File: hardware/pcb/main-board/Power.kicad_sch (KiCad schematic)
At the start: 59 parts, among them J1 Battery 22.2V IN, J16 Motor Driver, J2 Power Switch, J3 GND Spare Headers, J4 +V Spare Headers, Q1 DMMT5401 PNP, Q2 SSM3J332R, Q3 DMG2305UX-EV, Q4 DMMT5401 PNP, SW1 SW_SPST, U1 3.3V Buck, U2 12V Buck, U3 MAX42403AFLB+

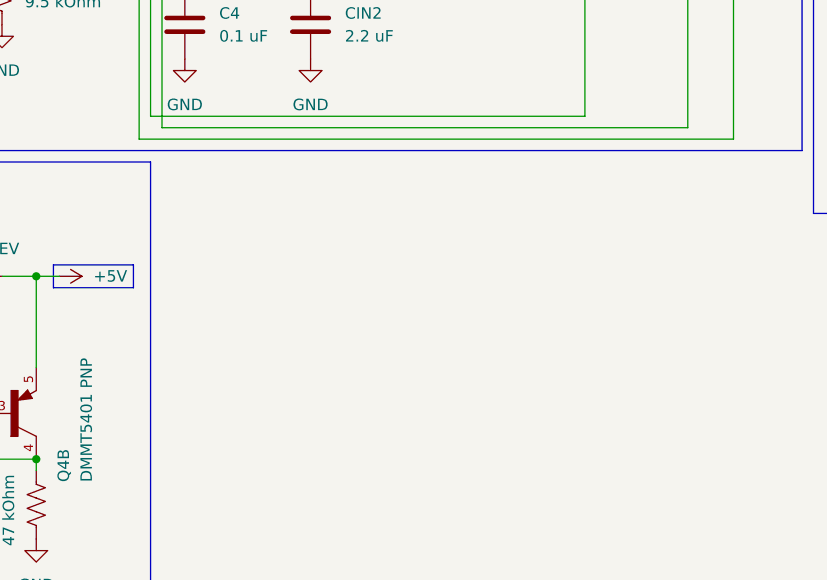
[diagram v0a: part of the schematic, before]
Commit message: Stepper drivers (real)
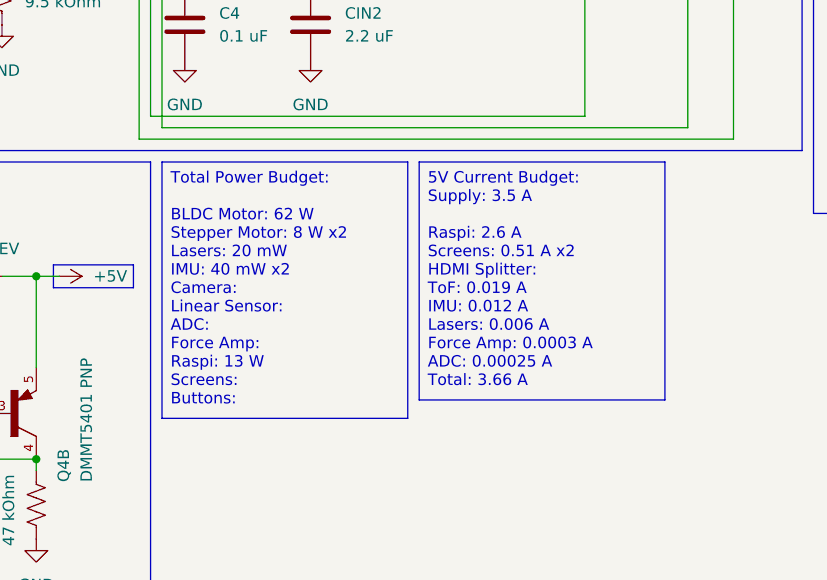
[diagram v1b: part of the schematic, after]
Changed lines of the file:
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@@
+		)
+	)
+	(text_box "Total Power Budget:\n\nBLDC Motor: 62 W\nStepper Motor: 8 W x2\nLasers: 20 mW\nIMU: 40 mW x2\nCamera:\nLinear Sensor:\nADC:\nForce Amp:\nRaspi: 13 W\nScreens:\nButtons:"
+		(exclude_from_sim no)
+		(at 58.42 124.46 0)
+		(size 27.305 28.4838)
+		(margins 0.9525 0.9525 0.9525 0.9525)
+		(stroke
+			(width 0)
+			(type solid)
+		)
+		(fill
+			(type none)
+		)
+		(effects
+			(font
+				(size 1.27 1.27)
+			)
+			(justify left top)
+		)
+	)
+	(text_box "5V Current Budget:\nSupply: 3.5 A\n\nRaspi: 2.6 A\nScreens: 0.51 A x2\nHDMI Splitter:\nToF: 0.019 A\nIMU: 0.012 A\nLasers: 0.006 A\nForce Amp: 0.0003 A\nADC: 0.00025 A\nTotal: 3.66 A"
+		(exclude_from_sim no)
+		(at 86.995 124.46 0)
+		(size 27.305 26.4392)
+		(margins 0.9525 0.9525 0.9525 0.9525)
+		(stroke
+			(width 0)
+			(type solid)
+		)
+		(fill
+			(type none)
+		)
+		(effects
+			(font
+				(size 1.27 1.27)
+			)
+			(justify left top)
 		)
 	)

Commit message: CAN-FD Transceiver Done
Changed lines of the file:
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@@
 		)
 	)
-	(text_box "5V Current Budget:\nSupply: 3.5 A\n\nRaspi: 2.6 A\nScreens: 0.51 A x2\nHDMI Splitter:\nToF: 0.019 A\nIMU: 0.012 A\nLasers: 0.006 A\nForce Amp: 0.0003 A\nADC: 0.00025 A\nTotal: 3.66 A"
+	(text_box "5V OLD Current Budget:\nSupply: 3.5 A\n\nRaspi: 2.6 A\nScreens: 0.51 A x2\nHDMI Splitter:\nToF: 0.019 A\nIMU: 0.012 A\nLasers: 0.006 A\nForce Amp: 0.0003 A\nADC: 0.00025 A\nTotal: 3.66 A"
 		(exclude_from_sim no)
 		(at 86.995 124.46 0)

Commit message: IMUs, I2C Pullups, Screen Power USB-C Ports
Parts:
- removed D6: SMCJ15A, Diode_SMD:D_SMC, symbol Device:D_Zener
- removed D7: SMCJ28A, Diode_SMD:D_SMC, symbol Device:D_Zener
- removed J2: Power Switch, Connector_AMASS:AMASS_XT30PW-F_1x02_P2.50mm_Horizontal, symbol Connector:Conn_01x02_Socket
- removed U2: 12V Buck, Converter_DCDC:Converter_DCDC_TRACO_TSR-1_THT, symbol Regulator_Switching:TSR_1-24120
- added J18: Screen 1 Power, symbol Connector:USB_C_Receptacle_PowerOnly_6P
- added J19: Screen 2 Power, symbol Connector:USB_C_Receptacle_PowerOnly_6P
- added R40, R41, R42, R43: 22 kOhm, Resistor_SMD:R_1206_3216Metric_Pad1.30x1.75mm_HandSolder, symbol Device:R_US
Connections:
- net +12V: no longer Contactor1.1, Flyback1.1 (K)
- net +5V: now also J18.A9 (VBUS), J18.B9 (VBUS), J19.A9 (VBUS), J19.B9 (VBUS), R40.2, R41.1, R42.1, R43.2
- net GND: now also J18.A12 (GND), J18.B12 (GND), J18.SH (SHIELD), J19.A12 (GND), J19.B12 (GND), J19.SH (SHIELD)
- new net: J18.A5 (CC1), R40.1
- new net: J18.B5 (CC2), R41.2
- new net: J19.A5 (CC1), R43.1
- new net: J19.B5 (CC2), R42.2
- new net To Contactor: Contactor1.1, Flyback1.1 (K)
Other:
- note added: "Screen Power Ports"

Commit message: USB ESD Prot.
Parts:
- added D14, D15: SMAJ6.0A, Diode_SMD:D_SMA, symbol Device:D_Zener
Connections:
- net +5V: now also R42.2, R43.1, D14.1 (K), D15.1 (K); no longer R42.1, R43.2
- net GND: now also D14.2 (A), D15.2 (A)
- net at J19.A5 (CC1): now also R42.1; no longer R43.1
- net at J19.B5 (CC2): now also R43.2; no longer R42.2
